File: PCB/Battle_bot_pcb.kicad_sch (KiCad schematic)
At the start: 59 parts, among them J2 USB_C_Receptacle_USB2.0, J4 Conn_01x02, J5 Conn_01x02, J6 Conn_01x02, J7 Conn_01x02, J8 Conn_01x02, J9 Conn_01x04, SW1 Reset, SW2 Boot, U2 TPS62172DSG, U3 USBLC6-2P6, U5 LSM6DS3, U6 DRV8833RTY, U7 LM1117LD-3.3, U8 ESP32-S3, Y1 40MHz

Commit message: Added Power multiplexer to schematic
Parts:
- removed C15: 10u, Capacitor_SMD:C_0603_1608Metric, symbol Device:C
- removed C16: 100n, Capacitor_SMD:C_0402_1005Metric, symbol Device:C
- removed U7: LM1117LD-3.3, Package_SON:WSON-8-1EP_4x4mm_P0.8mm_EP2.2x3mm, symbol Regulator_Linear:LM1117LD-3.3
- added Q1: AO3401A, Package_TO_SOT_SMD:SOT-23, symbol Transistor_FET:AO3401A
- added R11: 470k, Resistor_SMD:R_0402_1005Metric, symbol Device:R
- added U1: LTC4412xS6, Package_TO_SOT_SMD:TSOT-23-6, symbol Power_Management:LTC4412xS6
- C22: value 22u -> 10u; footprint Capacitor_SMD:C_0805_2012Metric -> Capacitor_SMD:C_0603_1608Metric
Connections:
- net +3.3V: now also R11.1
- net +5V: now also C11.1, C23.1, U2.2 (VIN), U2.3 (EN), Q1.2 (S), U1.6 (SENSE)
- net +BATT: now also Q1.3 (D), U1.1 (VIN); no longer C11.1, C23.1, U2.2 (VIN), U2.3 (EN)
- net GND: now also U1.2 (GND), U1.3 (CTL)
- net IN1: no longer U6.14 (AIN1)
- net IN2: no longer U6.13 (AIN2)
- net IN3: no longer U6.7 (BIN1)
- net IN4: no longer U6.8 (BIN2)
- new net: Q1.1 (G), U1.5 (GATE)
- new net STAT: R11.2, U1.4 (STAT)
- no-connect marks 3 -> 10
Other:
- note added: "AISEN and BISEN shunt resistor power rating (if used) 1W minimum. Calculated from max IC current (1.5A RMS) through 0.2Ω: P = I²R = (1.5A)² × 0.2Ω = 0.45W continuous With peak current (2A): P = (2A)² × 0.2Ω = 0.8W peak 1W rating is safe margin over both continuous and peak dissipation"
- note added: "Check VDDA vs VDD"
- note added: "Check for correct crystal"
- note added: "Check this later'"
- note added: "Power Multiplexer"
- note added: "Step down regulator"
- note added: "USB-diff: W = 0.2mm S = 0.1 mm -> 88 Ohm even and 51 Ohm odd"
- note added: "check if battery and usb voltage need to be the same"
- note added: "configuration: 3.3v, 500mA"
- note added: "wifi/bluetooth antenna AN043: 50 Ohm impedance Matching network should match antenna impedance"
- note removed: "Battery Connection and Step down regulator"
- note removed: "Check for correct crustal"
- note removed: "wifi/bluetooth antenna"
- moved on the sheet: AE1, C1, C10, C12, C13, C14, C17, C18, C19, C2, C21, C22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

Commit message: Added schottky diode to power multiplexer to protect USB hardware
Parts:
- added D3: SS14, Diode_SMD:D_SMA, symbol Diode:SS14
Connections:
- net +3.3V: now also J9.1 (Pin_1)
- net +5V: now also D3.2 (A); no longer C11.1, C23.1, Q1.2 (S), U1.6 (SENSE), U2.2 (VIN), U2.3 (EN)
- net +BATT: no longer J9.1 (Pin_1)
- net STAT: now also U8.23 (GPIO17/ADC2_CH6)
- new net: C11.1, C23.1, D3.1 (K), Q1.2 (S), U1.6 (SENSE), U2.2 (VIN), U2.3 (EN)
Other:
- note removed: "check if battery and usb voltage need to be the same"
- moved on the sheet: C12, C13, C14, C17, C18, J2, J9, L3, R5, R6, R7, R8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

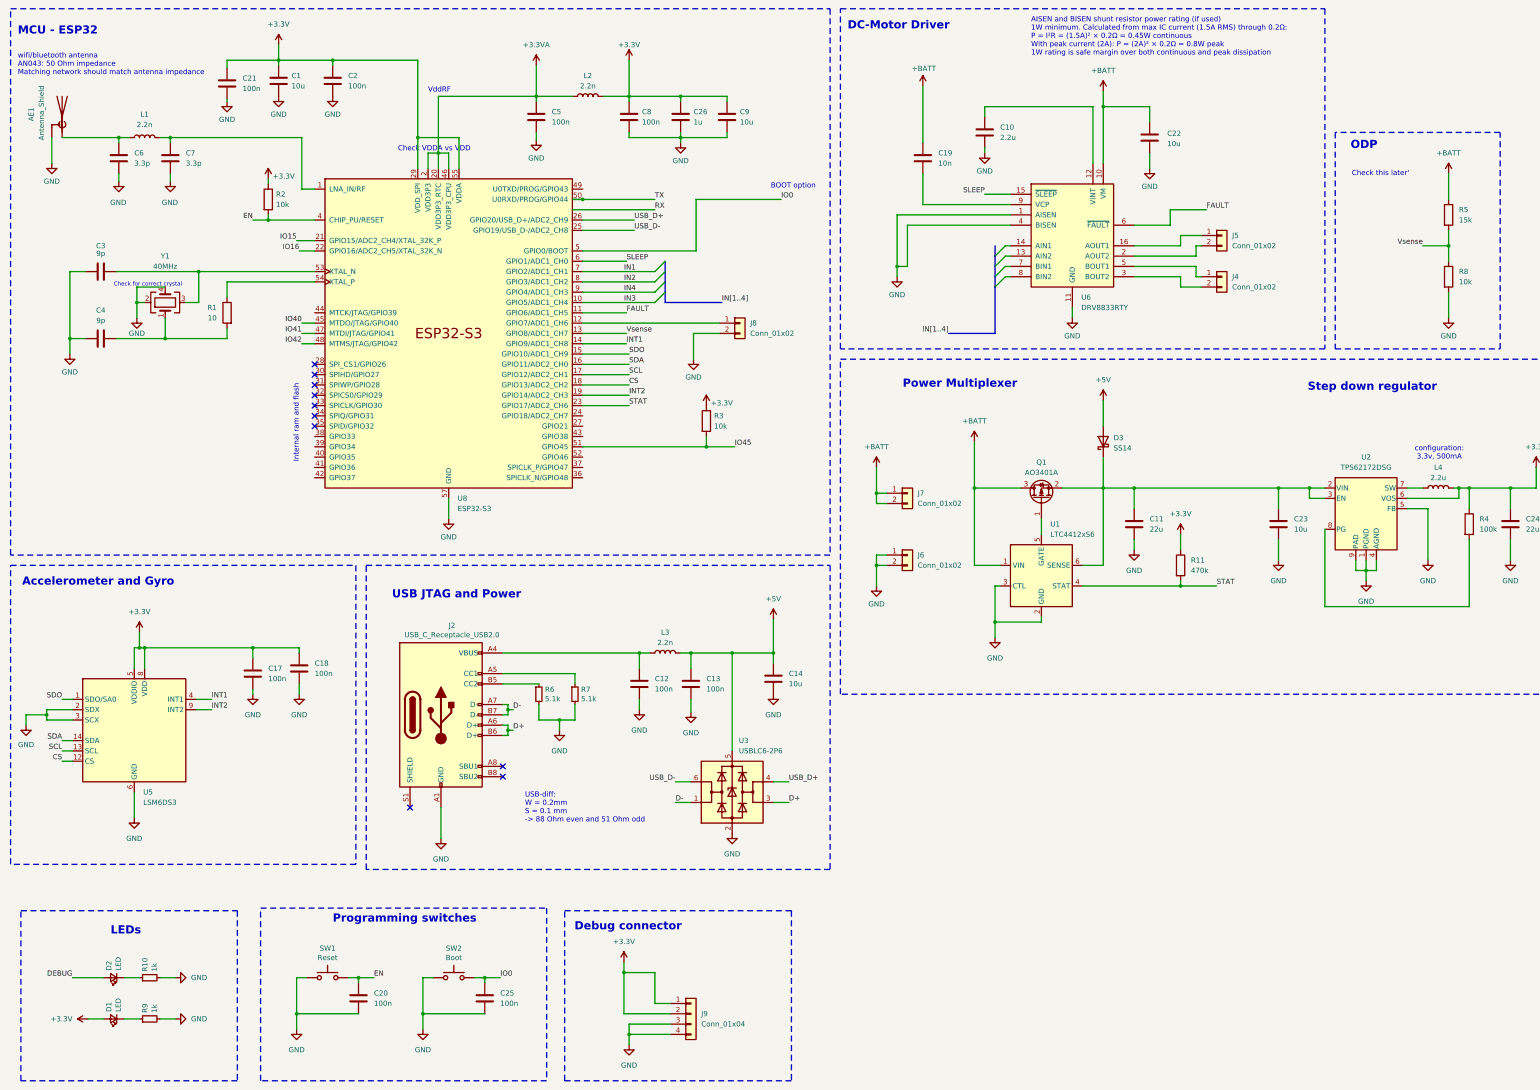
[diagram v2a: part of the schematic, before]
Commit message: added ESD Protection Diode near MCU
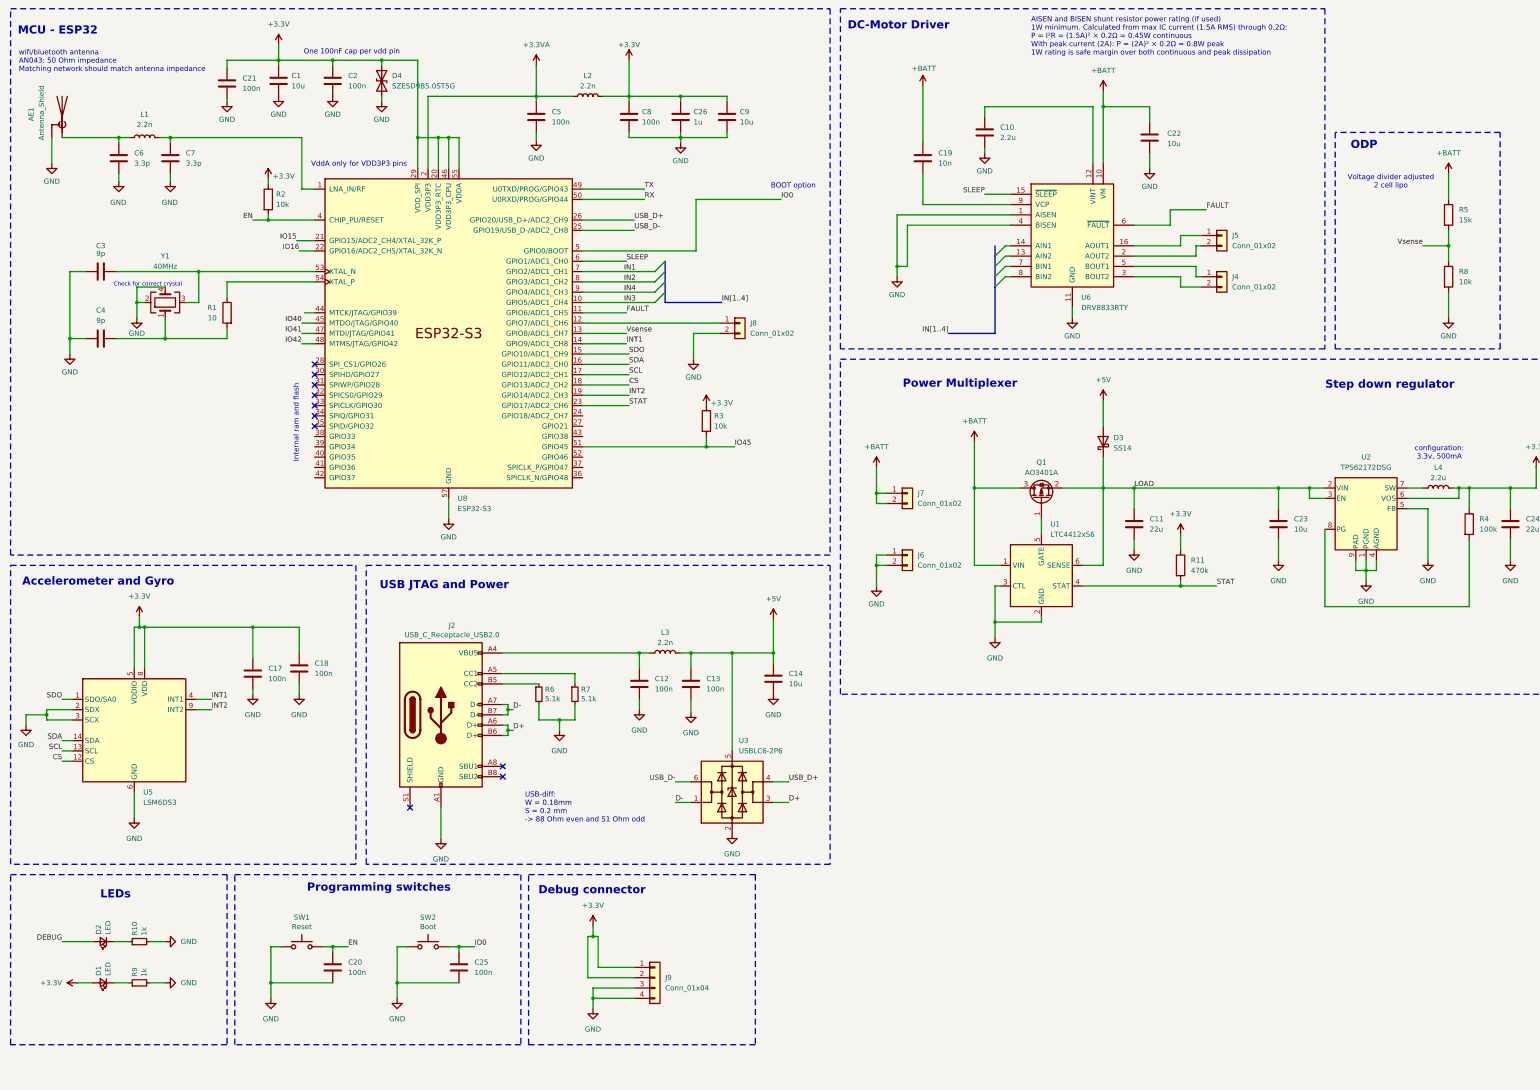
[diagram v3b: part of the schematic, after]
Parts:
- added D4: SZESD9B5.0ST5G, Diode_SMD:D_SOD-923, symbol Diode:SZESD9B5.0ST5G
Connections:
- net +3.3V: now also U8.20 (VDD3P3_RTC), U8.46 (VDD3P3_CPU), D4.2 (A2)
- net +3.3VA: no longer U8.20 (VDD3P3_RTC), U8.46 (VDD3P3_CPU)
- net GND: now also D4.1 (A1)
- net RX: now also U8.50 (U0RXD/PROG/GPIO44)
- net TX: now also U8.49 (U0TXD/PROG/GPIO43); no longer U8.50 (U0RXD/PROG/GPIO44)
- net LOAD: now reaches C11.1, C23.1, D3.1 (K), Q1.2 (S), U1.6 (SENSE), U2.2 (VIN), U2.3 (EN)
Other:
- note added: "One 100nF cap per vdd pin"
- note added: "USB-diff: W = 0.18mm S = 0.2 mm -> 88 Ohm even and 51 Ohm odd"
- note added: "VddA only for VDD3P3 pins"
- note added: "Voltage divider adjusted 2 cell lipo"
- note removed: "Check VDDA vs VDD"
- note removed: "Check this later'"
- note removed: "USB-diff: W = 0.2mm S = 0.1 mm -> 88 Ohm even and 51 Ohm odd"
- note removed: "VddRF"
- moved on the sheet: C20, C25, D1, D2, J9, R10, R9, SW1, SW2

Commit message: Small layout changes
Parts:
- added C25, C26: 100n, Capacitor_SMD:C_0402_1005Metric, symbol Device:C
- renumbered C3 to C1, C20 to C10, C25 to C11, C5 to C12, C8 to C13, C12 to C14, C26 to C15, C13 to C16, C9 to C17, C14 to C18, C4 to C2, C10 to C20, C11 to C21, C6 to C3, C7 to C4, C21 to C5, C17 to C6, C1 to C7, C18 to C8, C2 to C9, D2 to D1, D1 to D2, D4 to D3, D3 to D4, J2 to J1, J9 to J2, J8 to J3, J7 to J4, J6 to J5, J5 to J6, J4 to J7, R10 to R1, R8 to R10, R4 to R11, R9 to R2, R1 to R3, R2 to R4, R6 to R5, R7 to R6, R3 to R7, R11 to R8, R5 to R9, U5 to U1, U8 to U2, U1 to U4, U6 to U5, U2 to U6
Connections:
- net +3.3V: now also C25.1, C26.1
- net GND: now also C25.2, C26.2
- net IN1: now also U5.14 (AIN1)
- net IN2: now also U5.13 (AIN2)
- net IN3: now also U5.7 (BIN1)
- net IN4: now also U5.8 (BIN2)
- net STAT: no longer U2.23 (GPIO17/ADC2_CH6)
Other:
- note added: "USB-diff: W = 0.18mm S = 0.2 mm"
- note removed: "USB-diff: W = 0.18mm S = 0.2 mm -> 88 Ohm even and 51 Ohm odd"

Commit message: I/O header
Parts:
- added J8: Conn_01x04, Connector_PinHeader_2.54mm:PinHeader_1x04_P2.54mm_Vertical, symbol Connector_Generic:Conn_01x04
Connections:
- net DEBUG: now also U2.41 (GPIO36)
- net at U2.38 (GPIO33): now also J8.4 (Pin_4)
- net at U2.39 (GPIO34): now also J8.3 (Pin_3)
- net at U2.40 (GPIO35): now also J8.2 (Pin_2)
- net at U2.42 (GPIO37): now also J8.1 (Pin_1)
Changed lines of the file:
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@@
 	(wire
 		(pts
+			(xy 64.77 124.46) (xy 91.44 124.46)
+		)
+		(stroke
+			(width 0)
+			(type default)
+		)
+	)
+	(wire
+		(pts
 			(xy 168.91 39.37) (xy 168.91 38.1)
 		)
@@
 	(wire
 		(pts
+			(xy 81.28 129.54) (xy 91.44 129.54)
+		)
+		(stroke
+			(width 0)
+			(type default)
+		)
+	)
+	(wire
+		(pts
 			(xy 124.46 48.26) (xy 121.92 48.26)
 		)
@@
 	(wire
 		(pts
+			(xy 71.12 132.08) (xy 71.12 129.54)
+		)
+		(stroke
+			(width 0)
+			(type default)
+		)
+	)
+	(wire
+		(pts
 			(xy 170.18 255.27) (xy 158.75 255.27)
 		)
@@
 	(wire
 		(pts
+			(xy 64.77 127) (xy 91.44 127)
+		)
+		(stroke
+			(width 0)
+			(type default)
+		)
+	)
+	(wire
+		(pts
 			(xy 46.99 168.91) (xy 48.26 168.91)
 		)
@@
 	(wire
 		(pts
+			(xy 91.44 132.08) (xy 71.12 132.08)
+		)
+		(stroke
+			(width 0)
+			(type default)
+		)
+	)
+	(wire
+		(pts
 			(xy 157.48 99.06) (xy 168.275 99.06)
 		)
@@
 	(wire
 		(pts
+			(xy 71.12 129.54) (xy 64.77 129.54)
+		)
+		(stroke
+			(width 0)
+			(type default)
+		)
+	)
+	(wire
+		(pts
 			(xy 181.61 38.1) (xy 168.91 38.1)
 		)
@@
 	(wire
 		(pts
+			(xy 64.77 121.92) (xy 91.44 121.92)
+		)
+		(stroke
+			(width 0)
+			(type default)
+		)
+	)
+	(wire
+		(pts
 			(xy 270.51 167.64) (xy 270.51 166.37)
 		)
@@
 	(text "Internal ram and flash"
 		(exclude_from_sim no)
-		(at 87.63 128.27 90)
+		(at 88.138 120.396 90)
 		(effects
 			(font
@@
 		)
 	)
+	(label "DEBUG"
+		(at 81.28 129.54 180)
+		(fields_autoplaced yes)
+		(effects
+			(font
+				(size 1.27 1.27)
+			)
+			(justify right bottom)
+		)
+	)
 	(label "IN2"
 		(at 259.08 77.47 0)
@@
 					(unit 1)
 				)
+			)
+		)
+	)
+	(symbol
+		(lib_id "Connector_Generic:Conn_01x04")
+		(at 59.69 127 180)
+		(unit 1)
+		(exclude_from_sim no)
+		(in_bom yes)
+		(on_board yes)
+		(dnp no)
+		(fields_autoplaced yes)
+		(property "Reference" "J8"
+			(at 59.69 115.57 0)
+			(effects
+				(font
+					(size 1.27 1.27)
+				)
+			)
+		)
+		(property "Value" "Conn_01x04"
+			(at 59.69 118.11 0)
+			(effects
+				(font
+					(size 1.27 1.27)
+				)
+			)
+		)
+		(property "Footprint" "Connector_PinHeader_2.54mm:PinHeader_1x04_P2.54mm_Vertical"
+			(at 59.69 127 0)
+			(effects
+				(font
+					(size 1.27 1.27)
+				)
+				(hide yes)
+			)
+		)
+		(property "Datasheet" "~"
+			(at 59.69 127 0)
+			(effects
+				(font
+					(size 1.27 1.27)
+				)
+				(hide yes)
+			)
+		)
+		(property "Description" "Generic connector, single row, 01x04, script generated (kicad-library-utils/schlib/autogen/connector/)"
+			(at 59.69 127 0)
+			(effects
+				(font
+					(size 1.27 1.27)
+				)
+				(hide yes)
+			)
+		)
+		(pin "2"
+		)
+		(pin "3"
+		)
+		(pin "1"
+		)
+		(pin "4"
+		)
+		(instances
+			(project ""
+				(path "/d6203762-4d2e-4b90-86d1-ca295813f2e5"
+					(reference "J8")
+					(unit 1)
+				)

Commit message: Updated layout
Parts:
- removed AE1: Antenna_Shield, RF_Antenna:Texas_SWRA117D_2.4GHz_Left, symbol Device:Antenna_Shield
- removed C1, C2: 9p, Capacitor_SMD:C_0402_1005Metric, symbol Device:C
- removed C10, C11, C12, C13, C14, C16, C25, C26, C5, C6, C8, C9: 100n, Capacitor_SMD:C_0402_1005Metric, symbol Device:C
- removed C15: 1u, Capacitor_SMD:C_0603_1608Metric, symbol Device:C
- removed C17, C18, C22, C23, C7: 10u, Capacitor_SMD:C_0603_1608Metric, symbol Device:C
- removed C19: 10n, Capacitor_SMD:C_0402_1005Metric, symbol Device:C
- removed C20: 2.2u, Capacitor_SMD:C_0603_1608Metric, symbol Device:C
- removed C21, C24: 22u, Capacitor_SMD:C_0805_2012Metric, symbol Device:C
- removed C3, C4: 3.3p, Capacitor_SMD:C_0402_1005Metric, symbol Device:C
- removed D1, D2: LED, LED_SMD:LED_0805_2012Metric_Pad1.15x1.40mm_HandSolder, symbol Device:LED_Small
- removed D3: SZESD9B5.0ST5G, Diode_SMD:D_SOD-923, symbol Diode:SZESD9B5.0ST5G
- removed D4: SS14, Diode_SMD:D_SMA, symbol Diode:SS14
- removed J1: USB_C_Receptacle_USB2.0, Connector_USB:USB_C_Receptacle_HRO_TYPE-C-31-M-12, symbol Connector:USB_C_Receptacle_USB2.0
- removed J2, J8: Conn_01x04, Connector_PinHeader_2.54mm:PinHeader_1x04_P2.54mm_Vertical, symbol Connector_Generic:Conn_01x04
- removed J3, J4, J5, J6, J7: Conn_01x02, Connector_PinHeader_2.54mm:PinHeader_1x02_P2.54mm_Vertical, symbol Connector_Generic:Conn_01x02
- removed L1, L2: 2.2n, Inductor_SMD:L_0402_1005Metric, symbol Device:L
- removed L3: 2.2n, Inductor_SMD:L_0603_1608Metric, symbol Device:L
- removed L4: 2.2u, Inductor_SMD:L_0805_2012Metric, symbol Device:L
- removed Q1: AO3401A, Package_TO_SOT_SMD:SOT-23, symbol Transistor_FET:AO3401A
- removed R1, R2: 1k, Resistor_SMD:R_0402_1005Metric, symbol Device:R_Small
- removed R10, R4, R7: 10k, Resistor_SMD:R_0402_1005Metric, symbol Device:R
- removed R11: 100k, Resistor_SMD:R_0402_1005Metric, symbol Device:R
- removed R3: 10, Resistor_SMD:R_0402_1005Metric, symbol Device:R
- removed R5, R6: 5.1k, Resistor_SMD:R_0402_1005Metric, symbol Device:R_Small
- removed R8: 470k, Resistor_SMD:R_0402_1005Metric, symbol Device:R
- removed R9: 15k, Resistor_SMD:R_0402_1005Metric, symbol Device:R
- removed SW1: Reset, Button_Switch_SMD:SW_Push_SPST_NO_Alps_SKRK, symbol Switch:SW_Push
- removed SW2: Boot, Button_Switch_SMD:SW_Push_SPST_NO_Alps_SKRK, symbol Switch:SW_Push
- removed U1: LSM6DS3, Package_LGA:LGA-14_3x2.5mm_P0.5mm_LayoutBorder3x4y, symbol Sensor_Motion:LSM6DS3
- removed U2: ESP32-S3, Package_DFN_QFN:QFN-56-1EP_7x7mm_P0.4mm_EP5.6x5.6mm, symbol PCM_Espressif:ESP32-S3
- removed U3: USBLC6-2P6, Package_TO_SOT_SMD:SOT-666, symbol Power_Protection:USBLC6-2P6
- removed U4: LTC4412xS6, Package_TO_SOT_SMD:TSOT-23-6, symbol Power_Management:LTC4412xS6
- removed U5: DRV8833RTY, Package_DFN_QFN:Texas_RTY_WQFN-16-1EP_4x4mm_P0.65mm_EP2.1x2.1mm_ThermalVias, symbol Driver_Motor:DRV8833RTY
- removed U6: TPS62172DSG, Package_SON:WSON-8-1EP_2x2mm_P0.5mm_EP0.9x1.6mm_ThermalVias, symbol Regulator_Switching:TPS62172DSG
- removed Y1: 40MHz, Crystal:Crystal_SMD_3225-4Pin_3.2x2.5mm, symbol Device:Crystal_GND23
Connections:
- no-connect marks 10 -> 0
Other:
- added sheet IO (io.kicad_sch)
- added sheet MCU (mcu.kicad_sch)
- added sheet PWR (pwr.kicad_sch)
- note removed: "AISEN and BISEN shunt resistor power rating (if used) 1W minimum. Calculated from max IC current (1.5A RMS) through 0.2Ω: P = I²R = (1.5A)² × 0.2Ω = 0.45W continuous With peak current (2A): P = (2A)² × 0.2Ω = 0.8W peak 1W rating is safe margin over both continuous and peak dissipation"
- note removed: "Accelerometer and Gyro"
- note removed: "BOOT option"
- note removed: "Check for correct crystal"
- note removed: "DC-Motor Driver"
- note removed: "Debug connector"
- note removed: "Internal ram and flash"
- note removed: "LEDs"
- note removed: "MCU - ESP32"
- note removed: "ODP"
- note removed: "One 100nF cap per vdd pin"
- note removed: "Power Multiplexer"
- note removed: "Programming switches"
- note removed: "Step down regulator"
- note removed: "USB JTAG and Power"
- note removed: "USB-diff: W = 0.18mm S = 0.2 mm"
- note removed: "VddA only for VDD3P3 pins"
- note removed: "Voltage divider adjusted 2 cell lipo"
- note removed: "configuration: 3.3v, 500mA"
- note removed: "wifi/bluetooth antenna AN043: 50 Ohm impedance Matching network should match antenna impedance"

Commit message: Updates to README
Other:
- sheet IO renamed Motor Driver
- note added: "Functional Blocks"
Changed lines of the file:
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@@
+		)
+	)
+	(text "Functional Blocks"
+		(exclude_from_sim no)
+		(at 201.168 174.752 0)
+		(effects
+			(font
+				(face "KiCad Font")
+				(size 3 3)
+				(thickness 0.6)
+				(bold yes)
+			)
 		)
 	)
@@
 			(color 201 201 201 1.0000)
 		)
-		(property "Sheetname" "IO"
-			(at 177.8 82.55 0)
-			(effects
-				(font
+		(property "Sheetname" "Motor Driver"
+			(at 172.212 82.296 0)
+			(effects
+				(font
